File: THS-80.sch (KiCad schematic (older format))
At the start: 22 parts, among them J1 USB_B_Micro, J2 RC80 Bus, J3 RC80 Expansion, SW1 Reset, U1 MAX40203AUK, U2 DS1813R-5+T&R

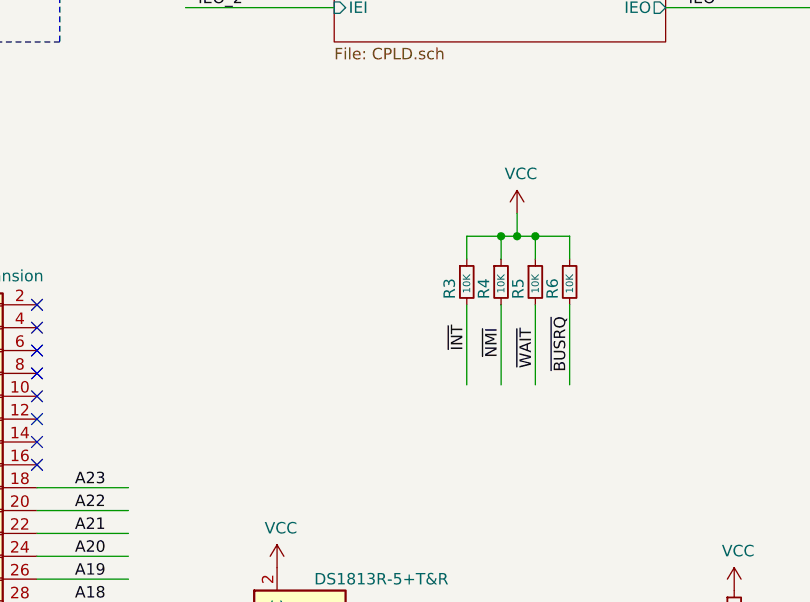
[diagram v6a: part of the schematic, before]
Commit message: Changed to resistor arrays, flipped to front-side
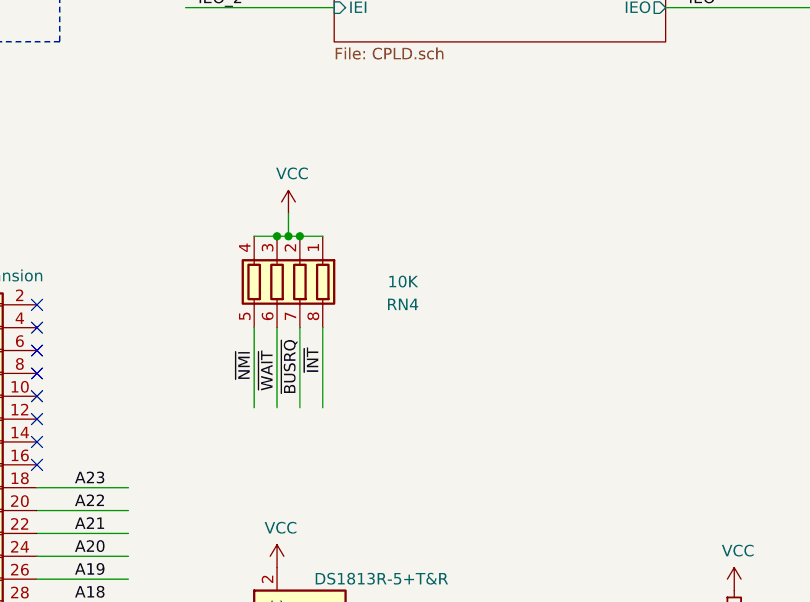
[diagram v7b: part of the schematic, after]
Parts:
- removed R3, R4, R5, R6: 10K, Resistor_SMD:R_0603_1608Metric_Pad1.05x0.95mm_HandSolder, symbol Device:R_Small
- added RN4: 10K, Resistor_SMD:R_Cat16-4, symbol Device:R_Pack04
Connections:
- wire segments 254 -> 250
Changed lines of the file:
@@
-	1    0    0    -1
-$EndComp
-$Comp
-L Device:R_Small R6
-U 1 1 5E47A0BC
-P 6280 3550
-AR Path="/5E47A0BC" Ref="R6"  Part="1"
-AR Path="/5D6224DC/5E47A0BC" Ref="R?"  Part="1"
-F 0 "R6" V 6205 3475 50  0000 L CNN
-F 1 "10K" V 6280 3500 32  0000 L CNN
-F 2 "Resistor_SMD:R_0603_1608Metric_Pad1.05x0.95mm_HandSolder" H 6280 3550 50  0001 C CNN
-F 3 "~" H 6280 3550 50  0001 C CNN
-	1    6280 3550
-	1    0    0    -1
-$EndComp
-$Comp
-L Device:R_Small R5
-U 1 1 5E47A0C2
-P 6130 3550
-AR Path="/5E47A0C2" Ref="R5"  Part="1"
-AR Path="/5D6224DC/5E47A0C2" Ref="R?"  Part="1"
-F 0 "R5" V 6055 3475 50  0000 L CNN
-F 1 "10K" V 6130 3500 32  0000 L CNN
-F 2 "Resistor_SMD:R_0603_1608Metric_Pad1.05x0.95mm_HandSolder" H 6130 3550 50  0001 C CNN
-F 3 "~" H 6130 3550 50  0001 C CNN
-	1    6130 3550
-	1    0    0    -1
-$EndComp
-$Comp
-L Device:R_Small R4
-U 1 1 5E47A0C8
-P 5980 3550
-AR Path="/5E47A0C8" Ref="R4"  Part="1"
-AR Path="/5D6224DC/5E47A0C8" Ref="R?"  Part="1"
-F 0 "R4" V 5905 3475 50  0000 L CNN
-F 1 "10K" V 5980 3500 32  0000 L CNN
-F 2 "Resistor_SMD:R_0603_1608Metric_Pad1.05x0.95mm_HandSolder" H 5980 3550 50  0001 C CNN
-F 3 "~" H 5980 3550 50  0001 C CNN
-	1    5980 3550
-	1    0    0    -1
-$EndComp
-$Comp
-L Device:R_Small R3
-U 1 1 5E47A0CE
-P 5830 3550
-AR Path="/5E47A0CE" Ref="R3"  Part="1"
-AR Path="/5D6224DC/5E47A0CE" Ref="R?"  Part="1"
-F 0 "R3" V 5755 3475 50  0000 L CNN
-F 1 "10K" V 5830 3500 32  0000 L CNN
-F 2 "Resistor_SMD:R_0603_1608Metric_Pad1.05x0.95mm_HandSolder" H 5830 3550 50  0001 C CNN
-F 3 "~" H 5830 3550 50  0001 C CNN
-	1    5830 3550
 	1    0    0    -1
 $EndComp
 Wire Wire Line
-	5830 3450 5830 3350
-Wire Wire Line
-	5830 3350 5980 3350
-Wire Wire Line
-	6280 3350 6280 3450
-Wire Wire Line
-	6130 3450 6130 3350
-Connection ~ 6130 3350
-Wire Wire Line
-	6130 3350 6280 3350
-Wire Wire Line
-	5980 3450 5980 3350
-Connection ~ 5980 3350
-Wire Wire Line
-	6280 3650 6280 4000
-Text Label 6280 3700 3    50   ~ 0
+	5100 3750 5100 4100
+Text Label 5100 3800 3    50   ~ 0
 ~BUSRQ
-Text Label 6130 3750 3    50   ~ 0
+Text Label 5000 3850 3    50   ~ 0
 ~WAIT
-Text Label 5980 3750 3    50   ~ 0
+Text Label 4900 3850 3    50   ~ 0
 ~NMI
-Text Label 5830 3850 1    50   ~ 0
+Text Label 5200 3950 1    50   ~ 0
 ~INT
 Wire Wire Line
-	6130 3650 6130 4000
+	5000 3750 5000 4100
 Wire Wire Line
-	5980 3650 5980 4000
+	4900 3750 4900 4100
 Wire Wire Line
-	5830 3650 5830 4000
+	5200 3750 5200 4100
 Text Label 5750 5200 0    50   ~ 0
 ~RST
@@
 	5000 5600 5000 5700
 Wire Wire Line
-	5980 3350 6050 3350
-Wire Wire Line
-	6050 3250 6050 3350
-Connection ~ 6050 3350
-Wire Wire Line
-	6050 3350 6130 3350
+	5050 3250 5050 3350
 $Comp
 L power:VCC #PWR0105
@@
 L power:VCC #PWR0137
 U 1 1 5E47A107
-P 6050 3250
-F 0 "#PWR0137" H 6050 3100 50  0001 C CNN
-F 1 "VCC" H 6067 3423 50  0000 C CNN
-F 2 "" H 6050 3250 50  0001 C CNN
-F 3 "" H 6050 3250 50  0001 C CNN
-	1    6050 3250
+P 5050 3250
+F 0 "#PWR0137" H 5050 3100 50  0001 C CNN
+F 1 "VCC" H 5067 3423 50  0000 C CNN
+F 2 "" H 5050 3250 50  0001 C CNN
+F 3 "" H 5050 3250 50  0001 C CNN
+	1    5050 3250
 	1    0    0    -1
 $EndComp
@@
 Wire Wire Line
 	7000 5100 7000 5200
+$Comp
+L Device:R_Pack04 RN?
+U 1 1 5E972F2D
+P 5000 3550
+AR Path="/5D70CA34/5E972F2D" Ref="RN?"  Part="1"
+AR Path="/5E972F2D" Ref="RN4"  Part="1"
+F 0 "RN4" H 4450 3650 50  0000 C CNN
+F 1 "10K" H 4450 3550 50  0000 C CNN
+F 2 "Resistor_SMD:R_Cat16-4" V 5475 3550 50  0001 C CNN
+F 3 "~" H 5000 3550 50  0001 C CNN
+	1    5000 3550
+	-1   0    0    1
+$EndComp
+Wire Wire Line
+	4900 3350 5000 3350
+Connection ~ 5000 3350
+Wire Wire Line
+	5000 3350 5050 3350
+Connection ~ 5100 3350
+Wire Wire Line
+	5100 3350 5200 3350
+Connection ~ 5050 3350
+Wire Wire Line
+	5050 3350 5100 3350
 $EndSCHEMATC

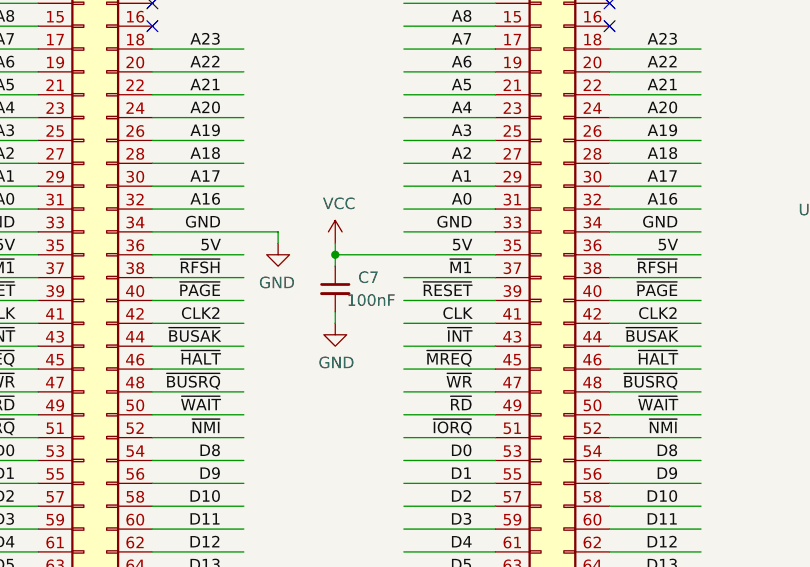
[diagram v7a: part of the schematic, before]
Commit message: removed extraneous components
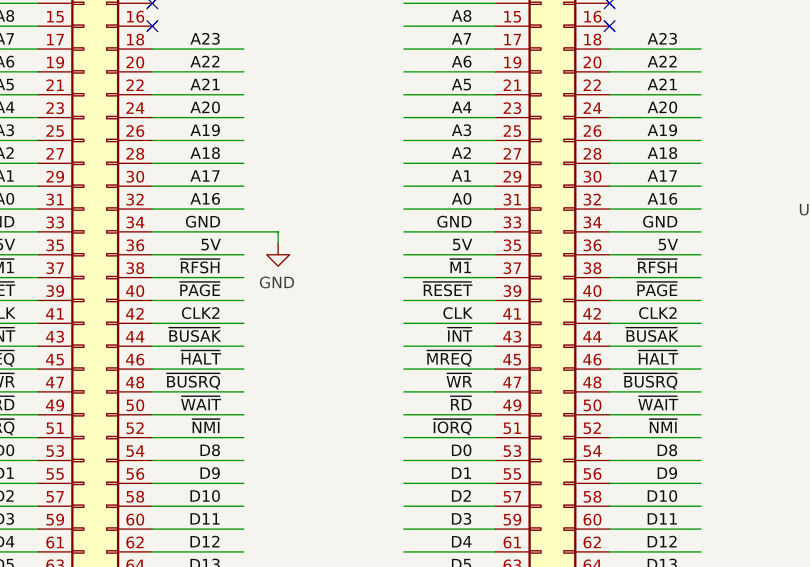
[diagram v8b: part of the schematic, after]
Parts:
- removed C7: 100nF, Capacitor_SMD:C_0603_1608Metric_Pad1.05x0.95mm_HandSolder, symbol Device:C_Small
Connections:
- wire segments 250 -> 247
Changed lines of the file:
@@
 CLK2
-Wire Wire Line
-	2750 5350 2750 5300
-$Comp
-L Device:C_Small C7
-U 1 1 5D9E460E
-P 2750 5500
-F 0 "C7" H 2850 5550 50  0000 L CNN
-F 1 "100nF" H 2800 5450 50  0000 L CNN
-F 2 "Capacitor_SMD:C_0603_1608Metric_Pad1.05x0.95mm_HandSolder" H 2788 5350 50  0001 C CNN
-F 3 "https://www.mouser.com/datasheet/2/212/KEM_C1002_X7R_SMD-1102033.pdf" H 2750 5500 50  0001 C CNN
-F 4 "KEMET" H -3900 -1200 50  0001 C CNN "MFR"
-F 5 "C0805C105K4RACTU" H -3900 -1200 50  0001 C CNN "MPN"
-F 6 "Mouser" H -3900 -1200 50  0001 C CNN "SPR"
-F 7 "80-C0805C105K4R" H -3900 -1200 50  0001 C CNN "SPN"
-F 8 "https://www.mouser.com/ProductDetail/KEMET/C0805C105K8RAC7210?qs=sGAEpiMZZMs0AnBnWHyRQOf5HOpVaXbh6p7WVhSDTqQ%3D" H -3900 -1200 50  0001 C CNN "SPURL"
-	1    2750 5500
-	1    0    0    -1
-$EndComp
-Wire Wire Line
-	2750 5400 2750 5350
-Wire Wire Line
-	2750 5600 2750 5650
-$Comp
-L power:GND #PWR013
-U 1 1 5D9E4616
-P 2750 5650
-AR Path="/5D9E4616" Ref="#PWR013"  Part="1"
-AR Path="/5CB63856/5D9E4616" Ref="#PWR?"  Part="1"
-AR Path="/5CB5AB00/5CB63856/5D9E4616" Ref="#PWR?"  Part="1"
-F 0 "#PWR013" H 2750 5400 50  0001 C CNN
-F 1 "GND" H 2755 5477 50  0000 C CNN
-F 2 "" H 2750 5650 50  0001 C CNN
-F 3 "" H 2750 5650 50  0001 C CNN
-	1    2750 5650
-	1    0    0    -1
-$EndComp
-Wire Wire Line
-	2750 5350 3450 5350
-Connection ~ 2750 5350
 Wire Wire Line
 	700  1850 950  1850
@@
 Text Label 3650 1250 2    50   ~ 0
 5V
-$Comp
-L power:VCC #PWR0101
-U 1 1 5DBC97DC
-P 2750 5300
-F 0 "#PWR0101" H 2750 5150 50  0001 C CNN
-F 1 "VCC" H 2767 5473 50  0000 C CNN
-F 2 "" H 2750 5300 50  0001 C CNN
-F 3 "" H 2750 5300 50  0001 C CNN
-	1    2750 5300
-	1    0    0    -1
-$EndComp
 $Comp
 L power:VCC #PWR0103
@@
 Wire Wire Line
 	5050 3350 5100 3350
+Wire Wire Line
+	3050 5350 3450 5350
 $EndSCHEMATC
